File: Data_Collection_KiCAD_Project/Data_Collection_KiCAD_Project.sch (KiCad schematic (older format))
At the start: 3 parts

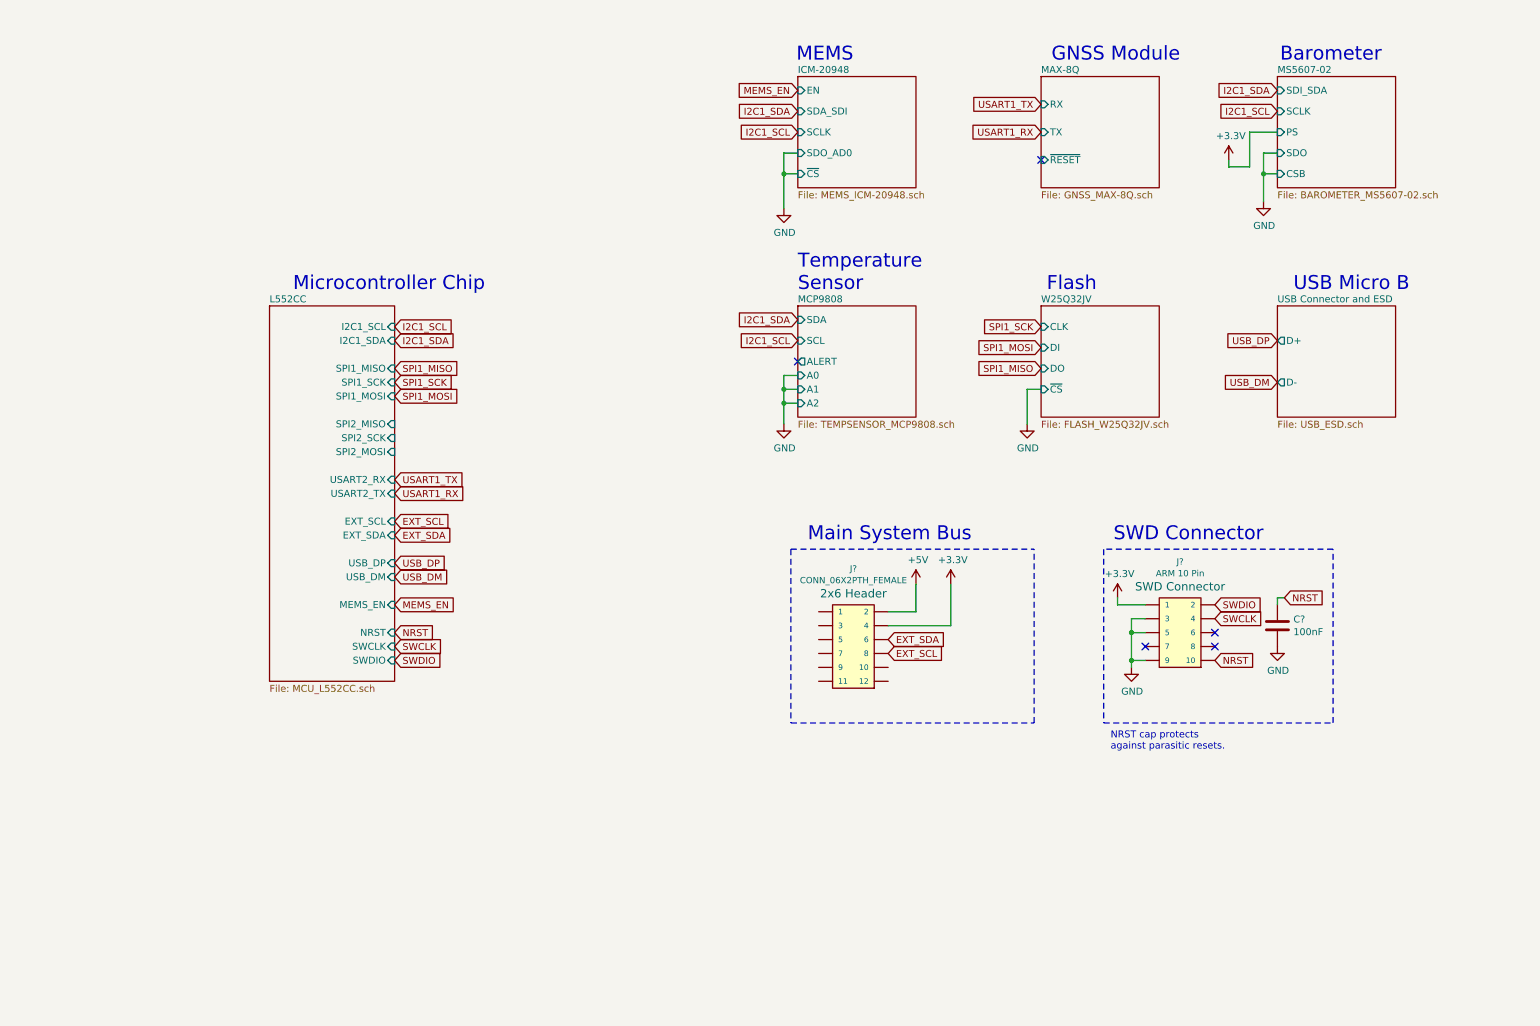
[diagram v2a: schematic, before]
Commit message: Schematic v1.0.3
Reorganized the main page to use bus lines.
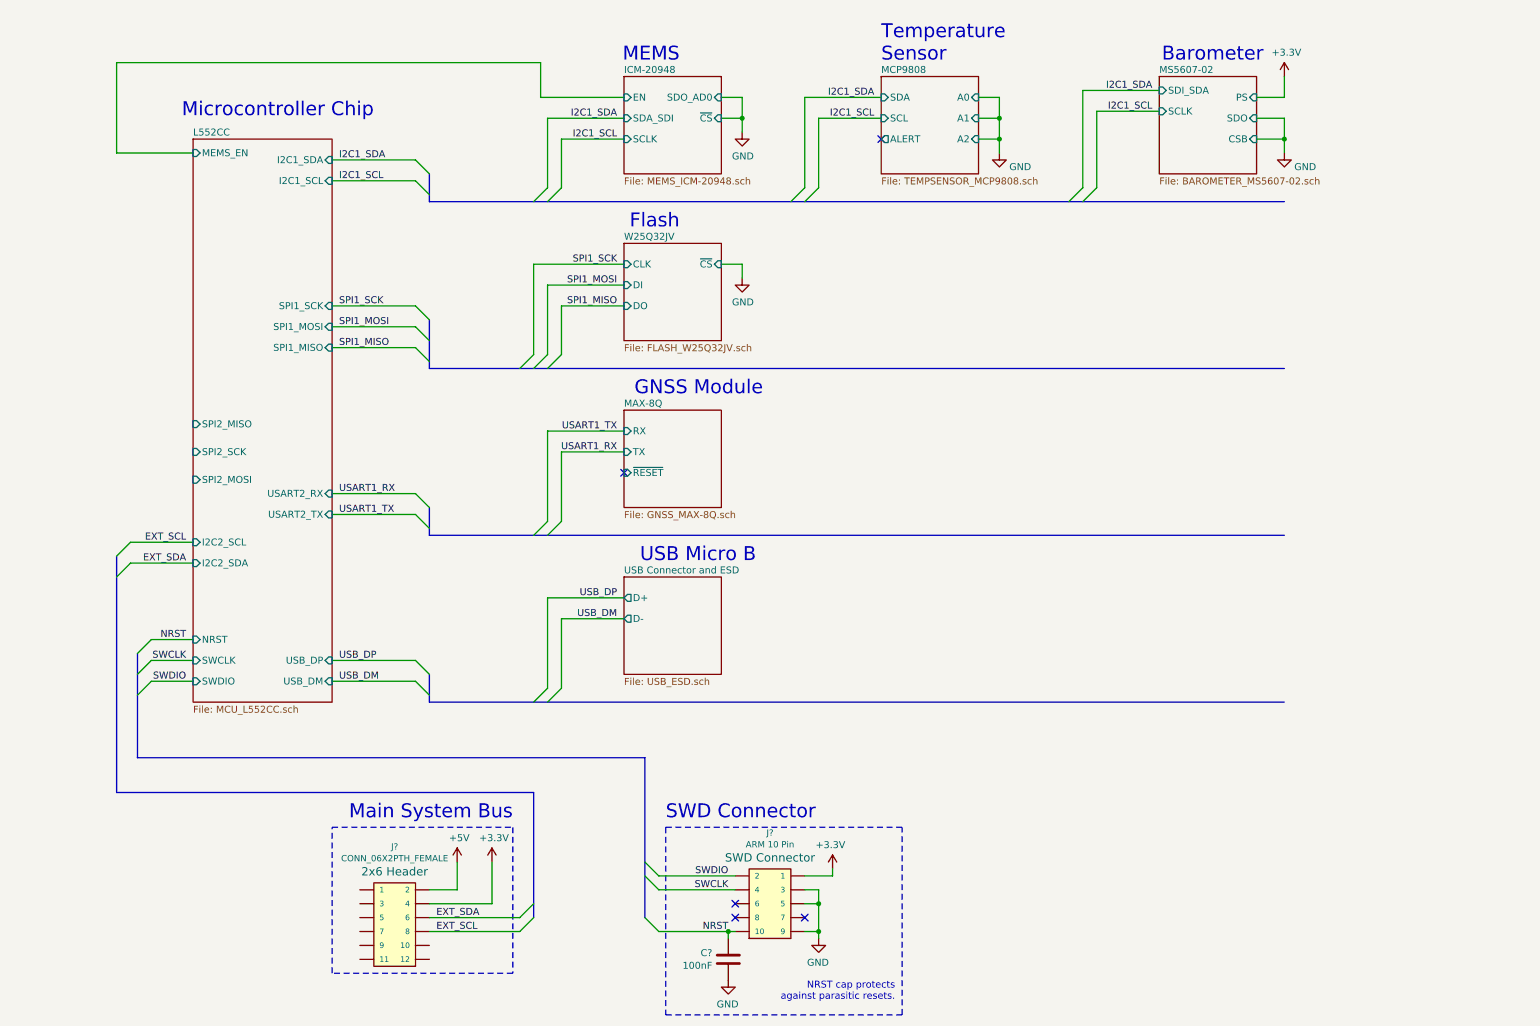
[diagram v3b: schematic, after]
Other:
- moved on the sheet: C?, J?

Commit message: Schematic v1.0.4
Added I2C addresses to MEMS, Temp Sensor, and Barometer on main schematic page.
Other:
- note added: "x18"
- note added: "x68"
- note added: "x77"
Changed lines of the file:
@@
 Title "Data Collection PCB Schematic"
 Date "2021-10-01"
-Rev "v1.0.3"
+Rev "v1.0.4"
 Comp "Missouri S&T Rocket Design Team '21 (Thomas Francois)"
 Comment1 "https://github.com/MSTRocketDesignTeam/Avionics-Data-Collection-PCB"
@@
 F5 "SDO_AD0" I R 5350 1150 50
 F6 "EN" I L 4650 1150 50
-$EndSheet
-$Sheet
-S 8500 1000 700  700
-U 615B3F6F
-F0 "MS5607-02" 50
-F1 "BAROMETER_MS5607-02.sch" 50
-F2 "SDI_SDA" I L 8500 1100 50
-F3 "SCLK" I L 8500 1250 50
-F4 "SDO" I R 9200 1300 50
-F5 "CSB" I R 9200 1450 50
-F6 "PS" I R 9200 1150 50
 $EndSheet
 $Comp
@@
 	7350 1300 7350 1150
 Wire Wire Line
-	9400 1550 9400 1450
-Wire Wire Line
-	9400 1450 9200 1450
-Wire Wire Line
-	9200 1300 9400 1300
-Wire Wire Line
-	9400 1300 9400 1450
-Connection ~ 9400 1450
-Wire Wire Line
 	9400 1000 9400 1150
 Wire Wire Line
@@
 Wire Notes Line
 	4950 6400 6650 6400
+Text Notes 5200 1700 0    50   ~ 0
+x68
+Text Notes 7050 1700 0    50   ~ 0
+x18
+Wire Wire Line
+	9400 1550 9400 1450
+Wire Wire Line
+	9400 1450 9200 1450
 Wire Bus Line
 	1000 4450 1000 6150
@@
 	4000 6150 4000 7050
 Wire Bus Line
+	4800 5900 4800 7050
+Wire Bus Line
+	1150 5150 1150 5900
+Wire Bus Line
 	3250 1700 3250 1900
 Wire Bus Line
+	3250 2750 3250 3100
+Wire Bus Line
 	3250 4100 3250 4300
 Wire Bus Line
 	3250 5300 3250 5500
 Wire Bus Line
+	3250 4300 9400 4300
+Wire Bus Line
 	3250 5500 9400 5500
 Wire Bus Line
-	3250 4300 9400 4300
-Wire Bus Line
-	3250 2750 3250 3100
-Wire Bus Line
-	1150 5150 1150 5900
-Wire Bus Line
-	4800 5900 4800 7050
-Wire Bus Line
 	3250 3100 9400 3100
 Wire Bus Line
 	3250 1900 9400 1900
+Connection ~ 9400 1450
+Wire Wire Line
+	9400 1300 9400 1450
+Wire Wire Line
+	9200 1300 9400 1300
+$Sheet
+S 8500 1000 700  700
+U 615B3F6F
+F0 "MS5607-02" 50
+F1 "BAROMETER_MS5607-02.sch" 50
+F2 "SDI_SDA" I L 8500 1100 50
+F3 "SCLK" I L 8500 1250 50
+F4 "SDO" I R 9200 1300 50
+F5 "PS" I R 9200 1150 50
+F6 "~CSB" I R 9200 1450 50
+$EndSheet
+Text Notes 9050 1700 0    50   ~ 0
+x77
 $EndSCHEMATC

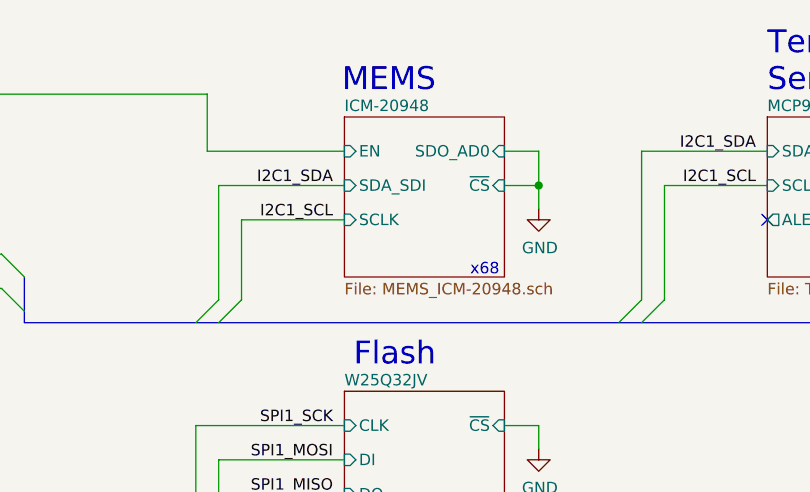
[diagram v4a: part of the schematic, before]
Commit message: Schematic v1.0.5
Added 64G capable Accelerometer.
Replaced ICM-20948 with BNO055 for 3.3V I2C compatibility.
Things to do: Add I2C pullup resistors for entire bus, Route INT pins to uC.
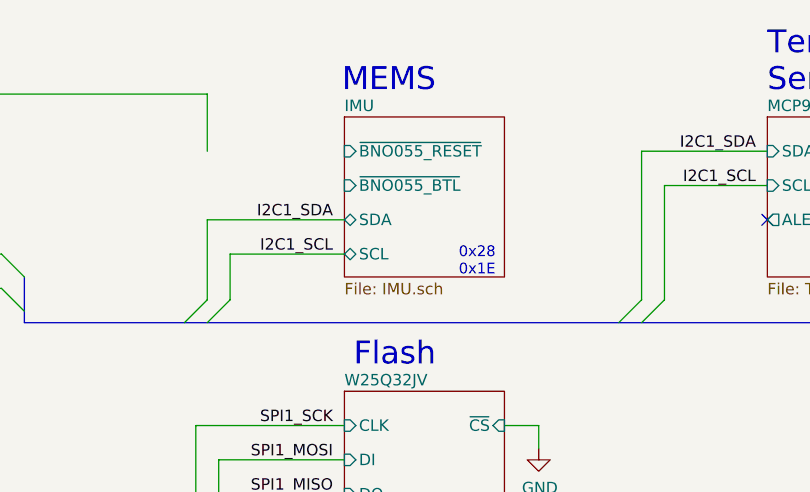
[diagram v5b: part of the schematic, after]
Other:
- note added: "0x28\n0x1E"
- note removed: "x68"
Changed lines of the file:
@@
 Text Notes 6600 7650 2    50   ~ 0
 NRST cap protects\nagainst parasitic resets.
-$Sheet
-S 4650 1000 700  700
-U 615A5159
-F0 "ICM-20948" 50
-F1 "MEMS_ICM-20948.sch" 50
-F2 "SDA_SDI" I L 4650 1300 50
-F3 "SCLK" I L 4650 1450 50
-F4 "~CS" I R 5350 1300 50
-F5 "SDO_AD0" I R 5350 1150 50
-F6 "EN" I L 4650 1150 50
-$EndSheet
-$Comp
-L power:GND #PWR?
-U 1 1 616A9A00
-P 5500 1400
-F 0 "#PWR?" H 5500 1150 50  0001 C CNN
-F 1 "GND" H 5505 1227 50  0000 C CNN
-F 2 "" H 5500 1400 50  0001 C CNN
-F 3 "" H 5500 1400 50  0001 C CNN
-	1    5500 1400
-	1    0    0    -1
-$EndComp
 $Comp
 L power:GND #PWR?
@@
 Flash
 Entry Wire Line
-	4000 1900 4100 1800
-Entry Wire Line
-	4100 1900 4200 1800
-Entry Wire Line
 	5850 1900 5950 1800
 Entry Wire Line
@@
 Entry Wire Line
 	7950 1900 8050 1800
-Text Label 4600 1300 2    50   ~ 0
+Text Label 4600 1450 2    50   ~ 0
 I2C1_SDA
-Text Label 4600 1450 2    50   ~ 0
+Text Label 4600 1600 2    50   ~ 0
 I2C1_SCL
 Text Label 6450 1150 2    50   ~ 0
@@
 Text Label 4600 2350 2    50   ~ 0
 SPI1_SCK
-Wire Wire Line
-	4200 1450 4650 1450
-Wire Wire Line
-	4100 1300 4650 1300
 Wire Wire Line
 	5950 1150 6500 1150
@@
 Wire Wire Line
 	9400 1150 9200 1150
-Wire Wire Line
-	5500 1400 5500 1300
-Wire Wire Line
-	5500 1150 5350 1150
-Wire Wire Line
-	5350 1300 5500 1300
-Connection ~ 5500 1300
-Wire Wire Line
-	5500 1300 5500 1150
 Text Label 4600 3700 2    50   ~ 0
 USART1_RX
@@
 Wire Wire Line
 	4000 2350 4000 3000
-Wire Wire Line
-	4100 1800 4100 1300
-Wire Wire Line
-	4200 1800 4200 1450
 Wire Wire Line
 	5950 1800 5950 1150
@@
 	4050 900  4050 1150
 Wire Wire Line
-	4050 1150 4650 1150
-Wire Wire Line
 	5500 2350 5350 2350
 Wire Wire Line
@@
 Wire Notes Line
 	4950 6400 6650 6400
-Text Notes 5200 1700 0    50   ~ 0
-x68
+Text Notes 5150 1700 0    47   ~ 0
+0x28\n0x1E
 Text Notes 7050 1700 0    50   ~ 0
 x18
@@
 Wire Wire Line
 	9400 1450 9200 1450
-Wire Bus Line
-	1000 4450 1000 6150
-Wire Bus Line
-	4000 6150 4000 7050
-Wire Bus Line
-	4800 5900 4800 7050
-Wire Bus Line
-	1150 5150 1150 5900
-Wire Bus Line
-	3250 1700 3250 1900
-Wire Bus Line
-	3250 2750 3250 3100
-Wire Bus Line
-	3250 4100 3250 4300
-Wire Bus Line
-	3250 5300 3250 5500
-Wire Bus Line
-	3250 4300 9400 4300
-Wire Bus Line
-	3250 5500 9400 5500
-Wire Bus Line
-	3250 3100 9400 3100
-Wire Bus Line
-	3250 1900 9400 1900
 Connection ~ 9400 1450
 Wire Wire Line
@@
 Text Notes 9050 1700 0    50   ~ 0
 x77
+$Sheet
+S 4650 1000 700  700
+U 615A5159
+F0 "IMU" 50
+F1 "IMU.sch" 50
+F2 "SDA" B L 4650 1450 50
+F3 "SCL" B L 4650 1600 50
+F4 "~BNO055_RESET" I L 4650 1150 50
+F5 "~BNO055_BTL" I L 4650 1300 50
+$EndSheet
+Entry Wire Line
+	3950 1900 4050 1800
+Entry Wire Line
+	4050 1900 4150 1800
+Wire Wire Line
+	4150 1800 4150 1600
+Wire Wire Line
+	4150 1600 4650 1600
+Wire Wire Line
+	4050 1800 4050 1450
+Wire Wire Line
+	4050 1450 4650 1450
+Wire Bus Line
+	1000 4450 1000 6150
+Wire Bus Line
+	4000 6150 4000 7050
+Wire Bus Line
+	3250 1700 3250 1900
+Wire Bus Line
+	3250 4100 3250 4300
+Wire Bus Line
+	3250 5300 3250 5500
+Wire Bus Line
+	3250 5500 9400 5500
+Wire Bus Line
+	3250 4300 9400 4300
+Wire Bus Line
+	3250 2750 3250 3100
+Wire Bus Line
+	1150 5150 1150 5900
+Wire Bus Line
+	4800 5900 4800 7050
+Wire Bus Line
+	3250 3100 9400 3100
+Wire Bus Line
+	3250 1900 9400 1900
 $EndSCHEMATC

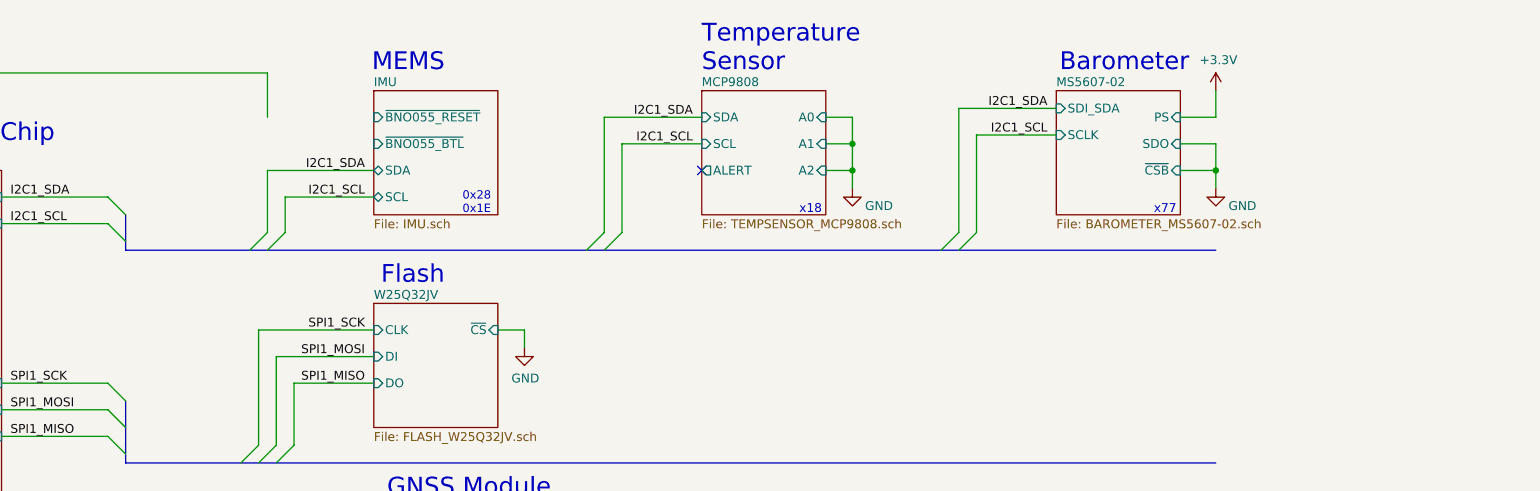
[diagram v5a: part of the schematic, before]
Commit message: Separated BNO055 and KX134
Separated the hierarchical sheets for the BNO055 IMU and KX134 High G-Accelerometer.
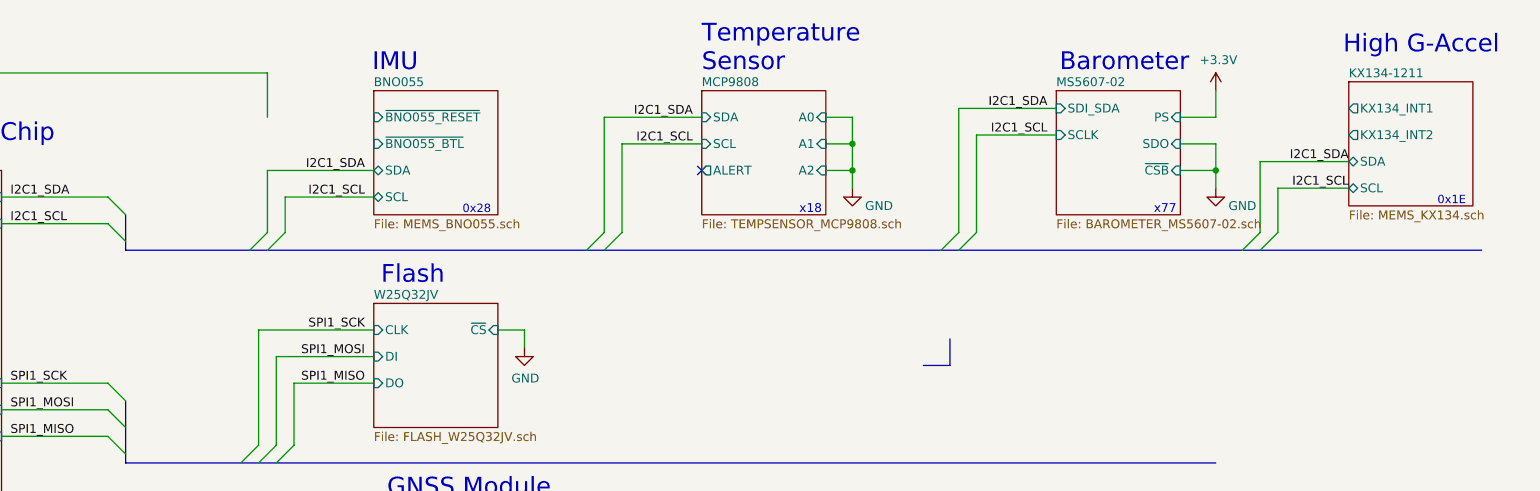
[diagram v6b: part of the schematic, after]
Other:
- note added: "0x1E"
- note added: "0x28\n"
- note added: "High G-Accel"
- note added: "IMU"
- note removed: "0x28\n0x1E"
- note removed: "MEMS"
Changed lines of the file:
@@
 $Descr A4 11693 8268
 encoding utf-8
-Sheet 1 8
+Sheet 1 9
 Title "Data Collection PCB Schematic"
 Date "2021-10-01"
@@
 Text Notes 6500 900  0    100  ~ 0
 Temperature\nSensor
-Text Notes 5050 900  2    100  ~ 0
-MEMS
+Text Notes 4900 900  2    100  ~ 0
+IMU
 Text Notes 9250 900  2    100  ~ 0
 Barometer
@@
 	4950 6400 6650 6400
 Text Notes 5150 1700 0    47   ~ 0
-0x28\n0x1E
+0x28\n
 Text Notes 7050 1700 0    50   ~ 0
 x18
@@
 Text Notes 9050 1700 0    50   ~ 0
 x77
+Entry Wire Line
+	3950 1900 4050 1800
+Entry Wire Line
+	4050 1900 4150 1800
+Wire Wire Line
+	4150 1800 4150 1600
+Wire Wire Line
+	4150 1600 4650 1600
+Wire Wire Line
+	4050 1800 4050 1450
+Wire Wire Line
+	4050 1450 4650 1450
 $Sheet
 S 4650 1000 700  700
 U 615A5159
-F0 "IMU" 50
-F1 "IMU.sch" 50
+F0 "BNO055" 50
+F1 "MEMS_BNO055.sch" 50
 F2 "SDA" B L 4650 1450 50
 F3 "SCL" B L 4650 1600 50
@@
 F5 "~BNO055_BTL" I L 4650 1300 50
 $EndSheet
-Entry Wire Line
-	3950 1900 4050 1800
-Entry Wire Line
-	4050 1900 4150 1800
-Wire Wire Line
-	4150 1800 4150 1600
-Wire Wire Line
-	4150 1600 4650 1600
-Wire Wire Line
-	4050 1800 4050 1450
-Wire Wire Line
-	4050 1450 4650 1450
+$Sheet
+S 10150 950  700  700
+U 61678964
+F0 "KX134-1211" 50
+F1 "MEMS_KX134.sch" 50
+F2 "SDA" B L 10150 1400 50
+F3 "SCL" B L 10150 1550 50
+F4 "KX134_INT1" O L 10150 1100 50
+F5 "KX134_INT2" O L 10150 1250 50
+$EndSheet
+Text Notes 11000 800  2    100  ~ 0
+High G-Accel
+Wire Bus Line
+	7750 2550 7900 2550
+Wire Bus Line
+	7900 2550 7900 2400
+Entry Wire Line
+	9650 1900 9750 1800
+Text Label 10150 1400 2    50   ~ 0
+I2C1_SDA
+Text Label 10150 1550 2    50   ~ 0
+I2C1_SCL
+Text Notes 10650 1650 0    47   ~ 0
+0x1E
+Entry Wire Line
+	9550 1900 9650 1800
+Wire Wire Line
+	9750 1800 9750 1550
+Wire Wire Line
+	9750 1550 10150 1550
+Wire Wire Line
+	9650 1800 9650 1400
+Wire Wire Line
+	9650 1400 10150 1400
 Wire Bus Line
 	1000 4450 1000 6150
@@
 	3250 3100 9400 3100
 Wire Bus Line
-	3250 1900 9400 1900
+	3250 1900 10900 1900
 $EndSCHEMATC

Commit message: Formatting
Misc Formatting and CubeIDE configuration.
Also Added datasheets folder
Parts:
- added J?: Main Bus, 2X6, symbol SparkFun-Connectors:CONN_06X2PTH_FEMALE
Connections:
- net GND: now also J?.1, J?.4
- new net 3.3V: J?.3, J?.6
- new net 5V: J?.7, J?.8
- new net SCL: J?.5
- new net SDA: J?.2
- no-connect marks 5 -> 9
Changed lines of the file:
@@
 F0 "L552CC" 50
 F1 "MCU_L552CC.sch" 50
-F2 "MEMS_EN" I L 1550 1550 50
-F3 "I2C1_SCL" I R 2550 1750 50
-F4 "I2C1_SDA" I R 2550 1600 50
-F5 "SPI2_SCK" I L 1550 3700 50
-F6 "I2C2_SDA" I L 1550 4500 50
-F7 "I2C2_SCL" I L 1550 4350 50
-F8 "SPI2_MISO" I L 1550 3500 50
-F9 "SPI2_MOSI" I L 1550 3900 50
-F10 "SPI1_SCK" I R 2550 2650 50
-F11 "USART2_TX" I R 2550 4150 50
-F12 "USART2_RX" I R 2550 4000 50
-F13 "SPI1_MISO" I R 2550 2950 50
-F14 "SPI1_MOSI" I R 2550 2800 50
-F15 "USB_DM" I R 2550 5350 50
-F16 "USB_DP" I R 2550 5200 50
-F17 "SWDIO" I L 1550 5350 50
-F18 "SWCLK" I L 1550 5200 50
-F19 "NRST" I L 1550 5050 50
+F2 "I2C1_SCL" I R 2550 1750 50
+F3 "I2C1_SDA" I R 2550 1600 50
+F4 "SPI2_SCK" I L 1550 3700 50
+F5 "SPI2_MISO" I L 1550 3500 50
+F6 "SPI2_MOSI" I L 1550 3900 50
+F7 "SPI1_SCK" I R 2550 2650 50
+F8 "USART2_TX" I R 2550 4150 50
+F9 "USART2_RX" I R 2550 4000 50
+F10 "SPI1_MISO" I R 2550 2950 50
+F11 "SPI1_MOSI" I R 2550 2800 50
+F12 "USB_DM" I R 2550 5350 50
+F13 "USB_DP" I R 2550 5200 50
+F14 "SWDIO" I L 1550 5350 50
+F15 "SWCLK" I L 1550 5200 50
+F16 "NRST" I L 1550 5050 50
 $EndSheet
 Wire Wire Line
 	5400 7150 5450 7150
-Wire Wire Line
-	1550 1550 1000 1550
-Wire Wire Line
-	1000 1550 1000 900
-Wire Wire Line
-	1000 900  4050 900
-Wire Wire Line
-	4050 900  4050 1150
 Wire Wire Line
 	5500 2350 5350 2350
@@
 Text Notes 11000 800  2    100  ~ 0
 High G-Accel
-Wire Bus Line
-	7750 2550 7900 2550
-Wire Bus Line
-	7900 2550 7900 2400
 Entry Wire Line
 	9650 1900 9750 1800
@@
 Wire Wire Line
 	9650 1400 10150 1400
+$Comp
+L SparkFun-Connectors:CONN_06X2PTH_FEMALE J?
+U 1 1 617A50A2
+P 1400 7150
+F 0 "J?" H 1400 7710 45  0000 C CNN
+F 1 "Main Bus" H 1400 7626 45  0000 C CNN
+F 2 "2X6" H 1400 7600 20  0001 C CNN
+F 3 "" H 1400 7150 50  0001 C CNN
+F 4 "2x6 Header" H 1400 7531 60  0000 C CNN "Field4"
+	1    1400 7150
+	1    0    0    -1
+$EndComp
+Text Label 1650 7000 0    50   ~ 0
+GND
+Text Label 1150 6900 2    50   ~ 0
+GND
+Text Label 1150 7200 2    50   ~ 0
+5V
+Text Label 1650 7200 0    50   ~ 0
+5V
+Text Label 1650 7100 0    50   ~ 0
+3.3V
+Text Label 1150 7000 2    50   ~ 0
+3.3V
+Text Label 1650 6900 0    50   ~ 0
+SDA
+Text Label 1150 7100 2    50   ~ 0
+SCL
+NoConn ~ 1150 7300
+NoConn ~ 1150 7400
+NoConn ~ 1650 7400
+NoConn ~ 1650 7300
 Wire Bus Line
 	1000 4450 1000 6150
